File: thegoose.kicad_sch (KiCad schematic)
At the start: 31 parts, among them U1 DRV8848, U2 DRV8848, U3 DRV8848, U4 AP64500SP-13

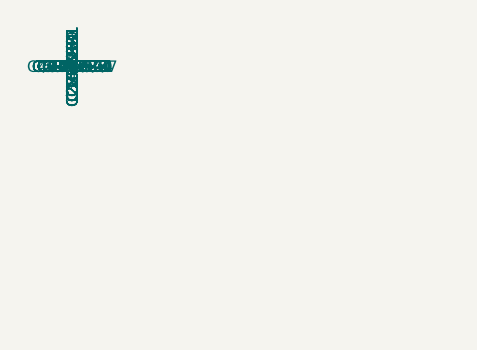
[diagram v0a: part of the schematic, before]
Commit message: Update LCSC part numbers
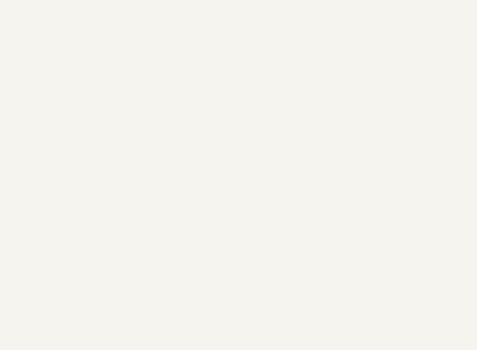
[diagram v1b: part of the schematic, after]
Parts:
- L1: footprint Inductor_SMD:L_1210_3225Metric_Pad1.42x2.65mm_HandSolder -> Inductor_SMD_Wurth:L_Wurth_WE-LQSH-4020

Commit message: Update BOM
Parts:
- C10, C15, C3, C6: LCSC Part # C272880 -> C380331
- C16: LCSC Part # C1847101 -> C25927664
- L1: LCSC Part # C167779 -> C7588667
- R27: LCSC Part # C856785 -> C228640
- R28: LCSC Part # C170028 -> C47115540
- U1, U2, U3: LCSC Part # C2863921 -> C131079
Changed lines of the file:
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@@
 			)
 		)
-		(property "LCSC Part #" "C272880"
+		(property "LCSC Part #" "C380331"
 			(at 81.2801 345.4401 0)
 			(effects
@@
 			)
 		)
-		(property "LCSC Part #" "C167779"
+		(property "LCSC Part #" "C7588667"
 			(at -81.2801 246.3801 0)
 			(effects
@@
 			)
 		)
-		(property "LCSC Part #" "C2863921"
+		(property "LCSC Part #" "C131079"
 			(at 43.1799 147.3201 0)
 			(effects
@@
 			)
 		)
-		(property "LCSC Part #" "C272880"
+		(property "LCSC Part #" "C380331"
 			(at -0.0001 -0.0001 0)
 			(effects
@@
 			)
 		)
-		(property "LCSC Part #" "C272880"
+		(property "LCSC Part #" "C380331"
 			(at -0.0001 -0.0001 0)
 			(effects
@@
 			)
 		)
-		(property "LCSC Part #" "C1847101"
+		(property "LCSC Part #" "C25927664"
 			(at 167.6401 360.6801 0)
 			(effects
@@
 			)
 		)
-		(property "LCSC Part #" "C856785"
+		(property "LCSC Part #" "C228640"
 			(at 195.5801 350.5201 0)
 			(effects
@@
 			)
 		)
-		(property "LCSC Part #" "C272880"
+		(property "LCSC Part #" "C380331"
 			(at -0.0001 -0.0001 0)
 			(effects
@@
 			)
 		)
-		(property "LCSC Part #" "C170028"
+		(property "LCSC Part #" "C47115540"
 			(at 167.6401 345.4401 0)
 			(effects
@@
 			)
 		)
-		(property "LCSC Part #" "C2863921"
+		(property "LCSC Part #" "C131079"
 			(at 114.2999 218.4401 0)
 			(effects
@@
 			)
 		)
-		(property "LCSC Part #" "C2863921"
+		(property "LCSC Part #" "C131079"
 			(at 186.6899 290.8301 0)
 			(effects

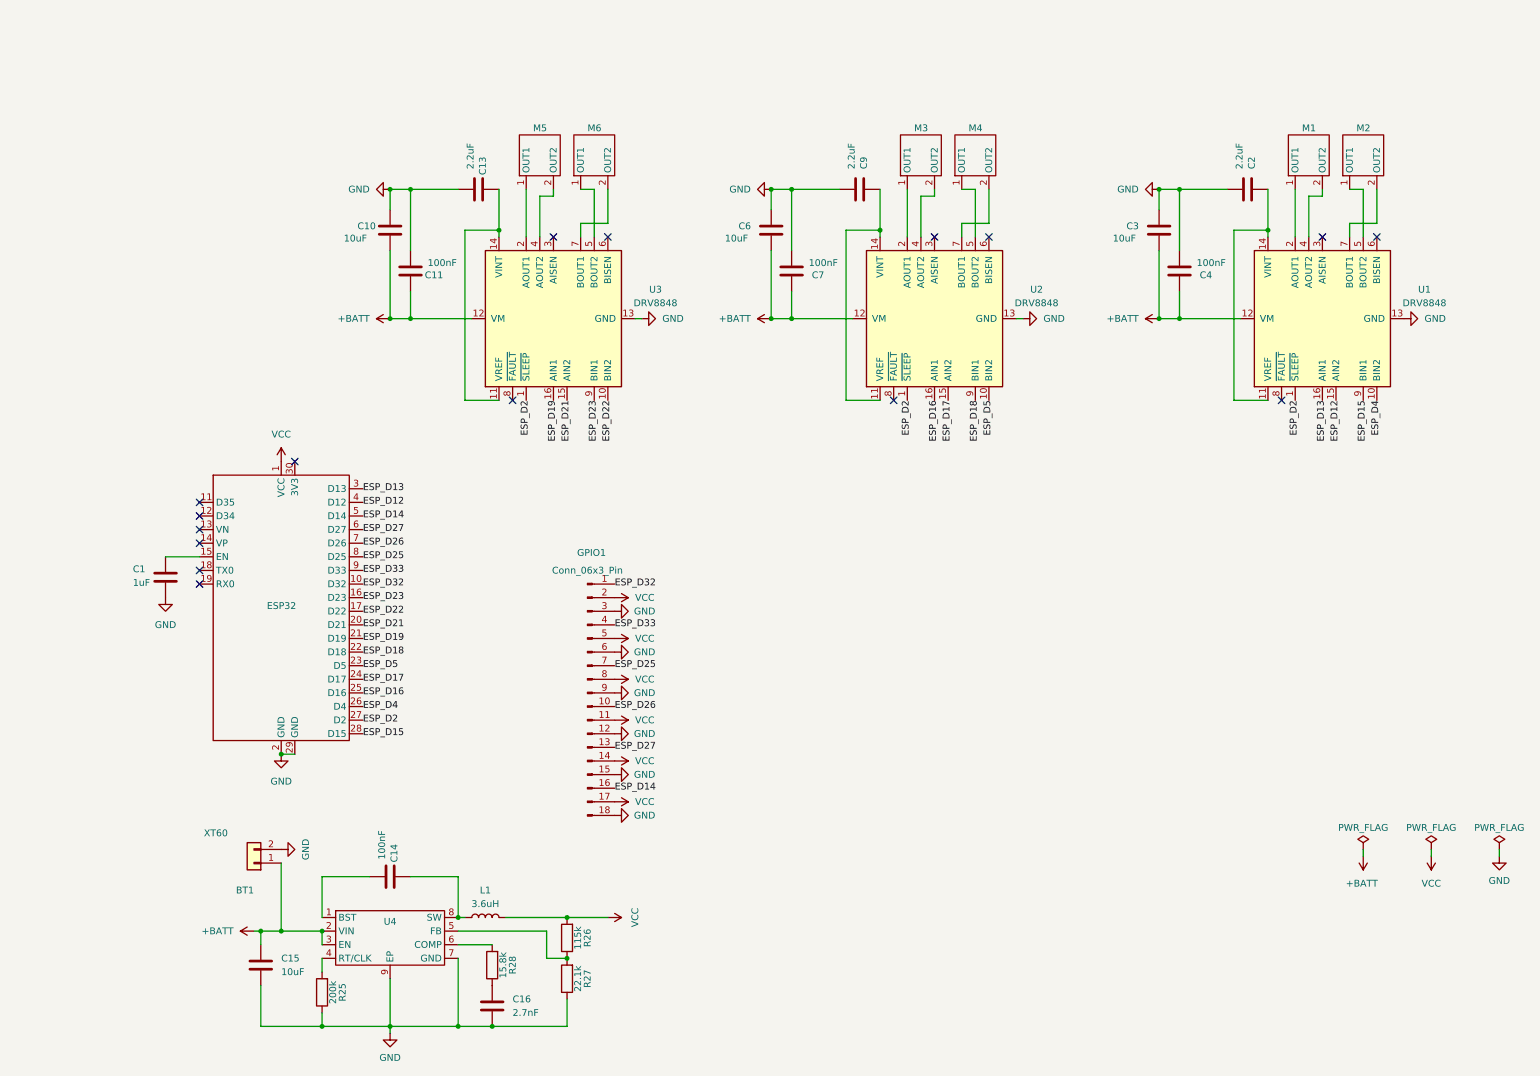
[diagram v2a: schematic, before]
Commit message: Switch footprint to two 1x15 header pins for ESP32
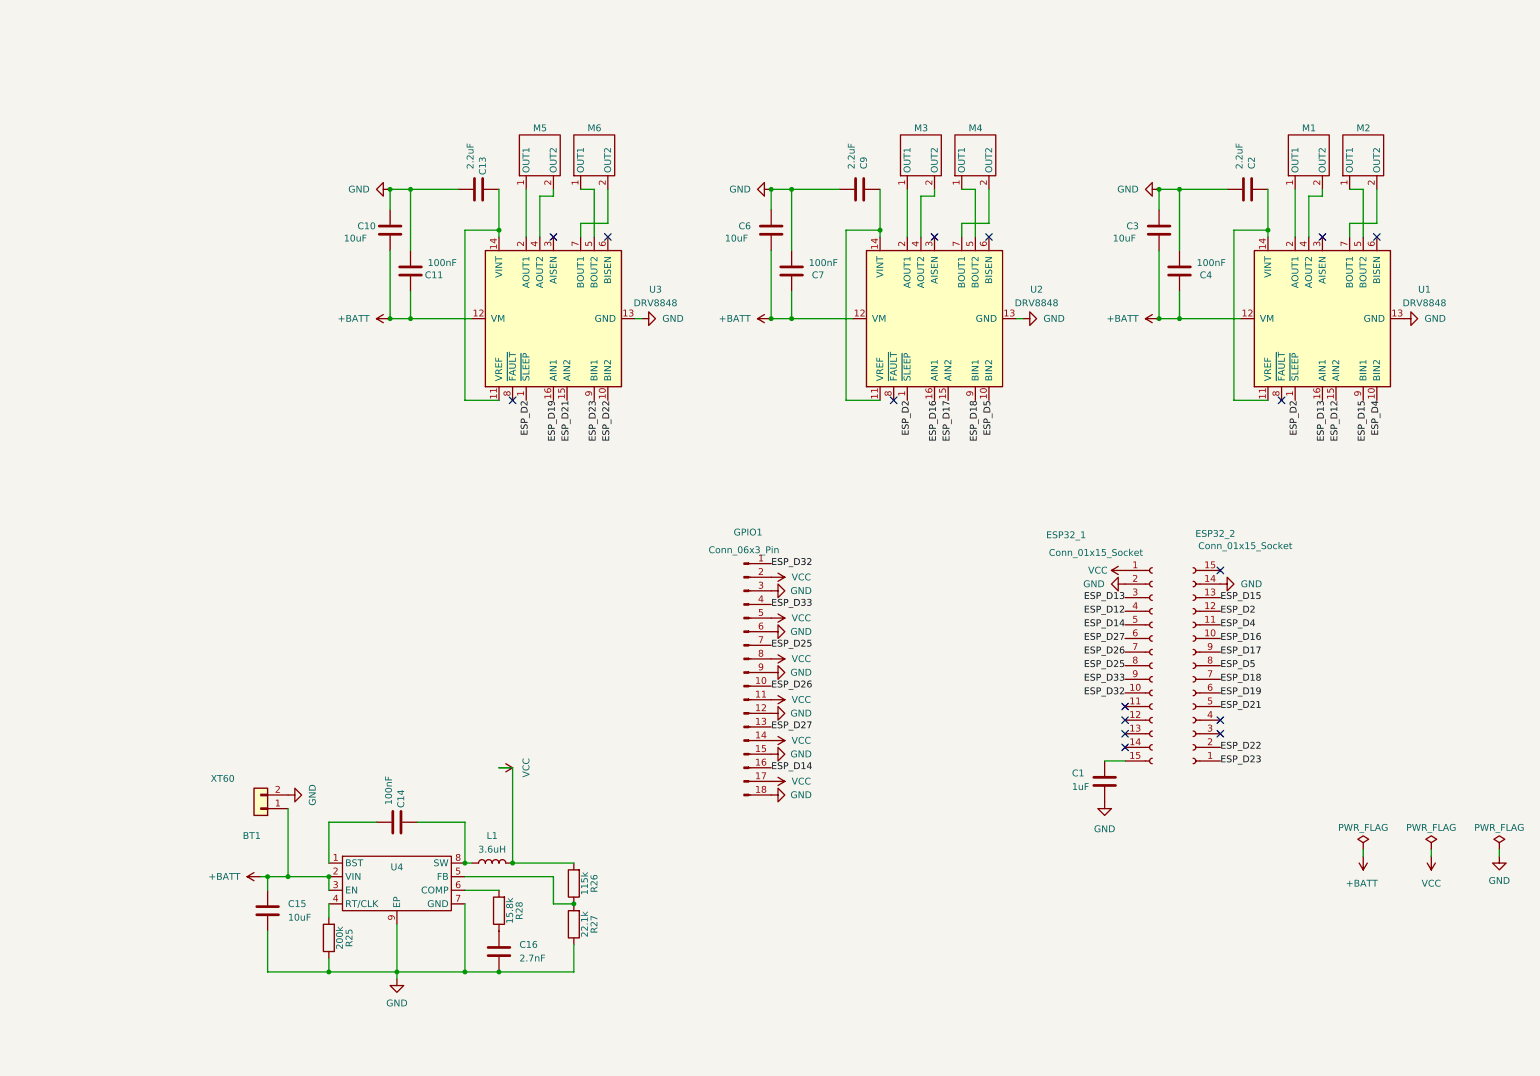
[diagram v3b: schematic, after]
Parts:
- removed ESP32: ESP32, hexy:ESP32, symbol hexyhustle:ESP32
- added ESP32_1, ESP32_2: Conn_01x15_Socket, Connector_PinSocket_2.54mm:PinSocket_1x15_P2.54mm_Vertical, symbol Connector:Conn_01x15_Socket
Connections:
- net ESP_D12: now also ESP32_1.4 (Pin_4)
- net ESP_D13: now also ESP32_1.3 (Pin_3)
- net ESP_D14: now also ESP32_1.5 (Pin_5)
- net ESP_D15: now also ESP32_2.13 (Pin_13)
- net ESP_D16: now also ESP32_2.10 (Pin_10)
- net ESP_D17: now also ESP32_2.9 (Pin_9)
- net ESP_D18: now also ESP32_2.7 (Pin_7)
- net ESP_D19: now also ESP32_2.6 (Pin_6)
- net ESP_D2: now also ESP32_2.12 (Pin_12)
- net ESP_D21: now also ESP32_2.5 (Pin_5)
- net ESP_D22: now also ESP32_2.2 (Pin_2)
- net ESP_D23: now also ESP32_2.1 (Pin_1)
- net ESP_D25: now also ESP32_1.8 (Pin_8)
- net ESP_D26: now also ESP32_1.7 (Pin_7)
- net ESP_D27: now also ESP32_1.6 (Pin_6)
- net ESP_D32: now also ESP32_1.10 (Pin_10)
- net ESP_D33: now also ESP32_1.9 (Pin_9)
- net ESP_D4: now also ESP32_2.11 (Pin_11)
- net ESP_D5: now also ESP32_2.8 (Pin_8)
- net GND: now also ESP32_1.2 (Pin_2), ESP32_2.14 (Pin_14)
- net VCC: now also ESP32_1.1 (Pin_1)
- net at C1.1: now also ESP32_1.15 (Pin_15)
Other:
- moved on the sheet: BT1, C1, C14, C15, C16, GPIO1, L1, R25, R26, R27, R28, U4

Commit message: Add female pin header LCSC part numbers
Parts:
- ESP32_1, ESP32_2: LCSC Part # (none) -> C2932676
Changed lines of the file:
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@@
+			)
+		)
+		(property "LCSC Part #" "C2932676"
+			(at 214.63 116.84 0)
+			(effects
+				(font
+					(size 1.27 1.27)
+				)
+				(hide yes)
 			)
 		)
@@
 			(at 207.01 116.84 0)
 			(effects
+				(font
+					(size 1.27 1.27)
+				)
+				(hide yes)
+			)
+		)
+		(property "LCSC Part #" "C2932676"
+			(at 207.01 116.84 0)
+			(effects

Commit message: Add extra capacitors to buck converter
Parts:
- added C12, C5, C8: 22uF, Capacitor_SMD:C_0805_2012Metric, symbol Device:C
- C1: footprint Capacitor_SMD:C_0805_2012Metric_Pad1.18x1.45mm_HandSolder -> Capacitor_SMD:C_0805_2012Metric; LCSC Part # C106837 -> C28323
- C10, C15, C3, C6: footprint Capacitor_SMD:C_0805_2012Metric_Pad1.18x1.45mm_HandSolder -> Capacitor_SMD:C_0805_2012Metric; LCSC Part # C380331 -> C15850
- C11, C14, C4, C7: footprint Capacitor_SMD:C_0805_2012Metric_Pad1.18x1.45mm_HandSolder -> Capacitor_SMD:C_0805_2012Metric; LCSC Part # C344180 -> C49678
- C13, C2, C9: footprint Capacitor_SMD:C_0805_2012Metric_Pad1.18x1.45mm_HandSolder -> Capacitor_SMD:C_0805_2012Metric; LCSC Part # C76638 -> C377773
- C16: footprint Capacitor_SMD:C_0805_2012Metric_Pad1.18x1.45mm_HandSolder -> Capacitor_SMD:C_0201_0603Metric
- U4: LCSC Part # C2070920 -> C1609
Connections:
- net GND: now also C12.2, C5.2, C8.2
- net VCC: now also C12.1, C5.1, C8.1

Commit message: Update all footprints
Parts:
- C16: footprint Capacitor_SMD:C_0201_0603Metric -> Capacitor_SMD:C_0402_1005Metric
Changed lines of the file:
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@@
 			)
 		)
-		(property "Footprint" "Capacitor_SMD:C_0201_0603Metric"
+		(property "Footprint" "Capacitor_SMD:C_0402_1005Metric"
 			(at 84.1248 166.37 0)
 			(effects

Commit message: Rework vias
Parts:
- C12, C5, C8: footprint Capacitor_SMD:C_0805_2012Metric -> Capacitor_SMD:C_0201_0603Metric; LCSC Part # (none) -> C59461
- C16: footprint Capacitor_SMD:C_0402_1005Metric -> Capacitor_SMD:C_0603_1608Metric; LCSC Part # C25927664 -> C302024
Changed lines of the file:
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@@
 			)
 		)
-		(property "Footprint" "Capacitor_SMD:C_0805_2012Metric"
+		(property "Footprint" "Capacitor_SMD:C_0201_0603Metric"
 			(at 100.33 146.3548 0)
 			(effects
@@
 			)
 		)
+		(property "LCSC Part #" "C59461"
+			(at 96.52 147.32 90)
+			(effects
+				(font
+					(size 1.27 1.27)
+				)
+				(hide yes)
+			)
+		)
 		(pin "1"
 		)
@@
 			)
 		)
-		(property "Footprint" "Capacitor_SMD:C_0805_2012Metric"
+		(property "Footprint" "Capacitor_SMD:C_0201_0603Metric"
 			(at 100.33 123.4948 0)
 			(effects
@@
 			)
 		)
+		(property "LCSC Part #" "C59461"
+			(at 96.52 124.46 90)
+			(effects
+				(font
+					(size 1.27 1.27)
+				)
+				(hide yes)
+			)
+		)
 		(pin "1"
 		)
@@
 			)
 		)
-		(property "Footprint" "Capacitor_SMD:C_0805_2012Metric"
+		(property "Footprint" "Capacitor_SMD:C_0201_0603Metric"
 			(at 100.33 134.9248 0)
 			(effects
@@
 			)
 		)
+		(property "LCSC Part #" "C59461"
+			(at 96.52 135.89 90)
+			(effects
+				(font
+					(size 1.27 1.27)
+				)
+				(hide yes)
+			)
+		)
 		(pin "1"
 		)
@@
 			)
 		)
-		(property "Footprint" "Capacitor_SMD:C_0402_1005Metric"
+		(property "Footprint" "Capacitor_SMD:C_0603_1608Metric"
 			(at 84.1248 166.37 0)
 			(effects
@@
 			)
 		)
-		(property "LCSC Part #" "C25927664"
+		(property "LCSC Part #" "C302024"
 			(at 168.9101 350.5201 0)
 			(effects

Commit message: Jark review
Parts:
- U4: LCSC Part # C1609 -> C2070920
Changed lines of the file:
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@@
 			)
 		)
-		(property "LCSC Part #" "C1609"
+		(property "LCSC Part #" "C2070920"
 			(at 1.2699 -10.1601 0)
 			(effects
